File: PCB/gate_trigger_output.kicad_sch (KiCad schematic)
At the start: 9 parts, among them J2 OUTa, J3 OUTb, Q2 BC547

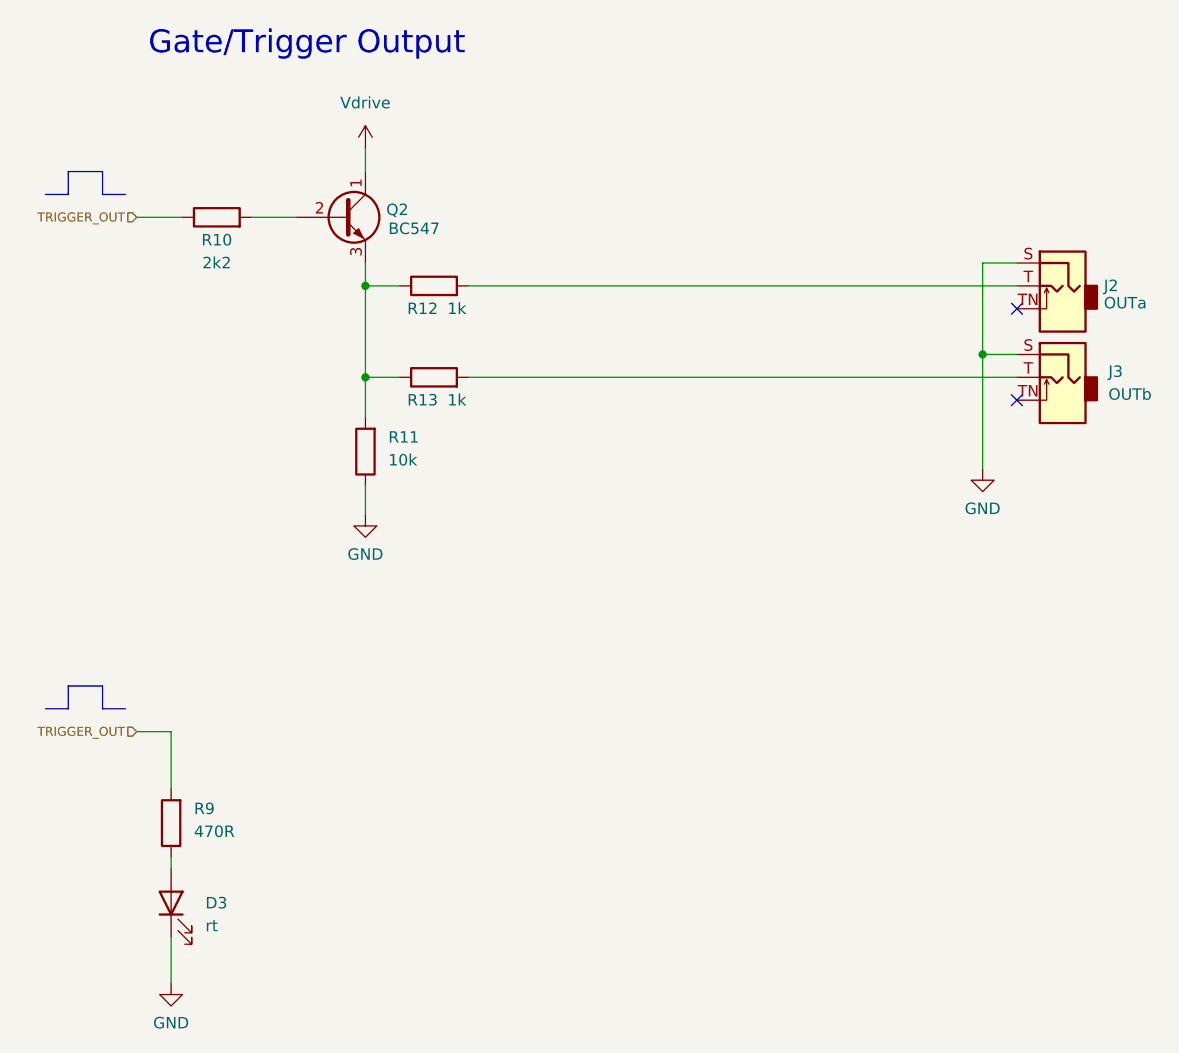
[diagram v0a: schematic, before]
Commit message: :memo: Geographically reannotate the PCB
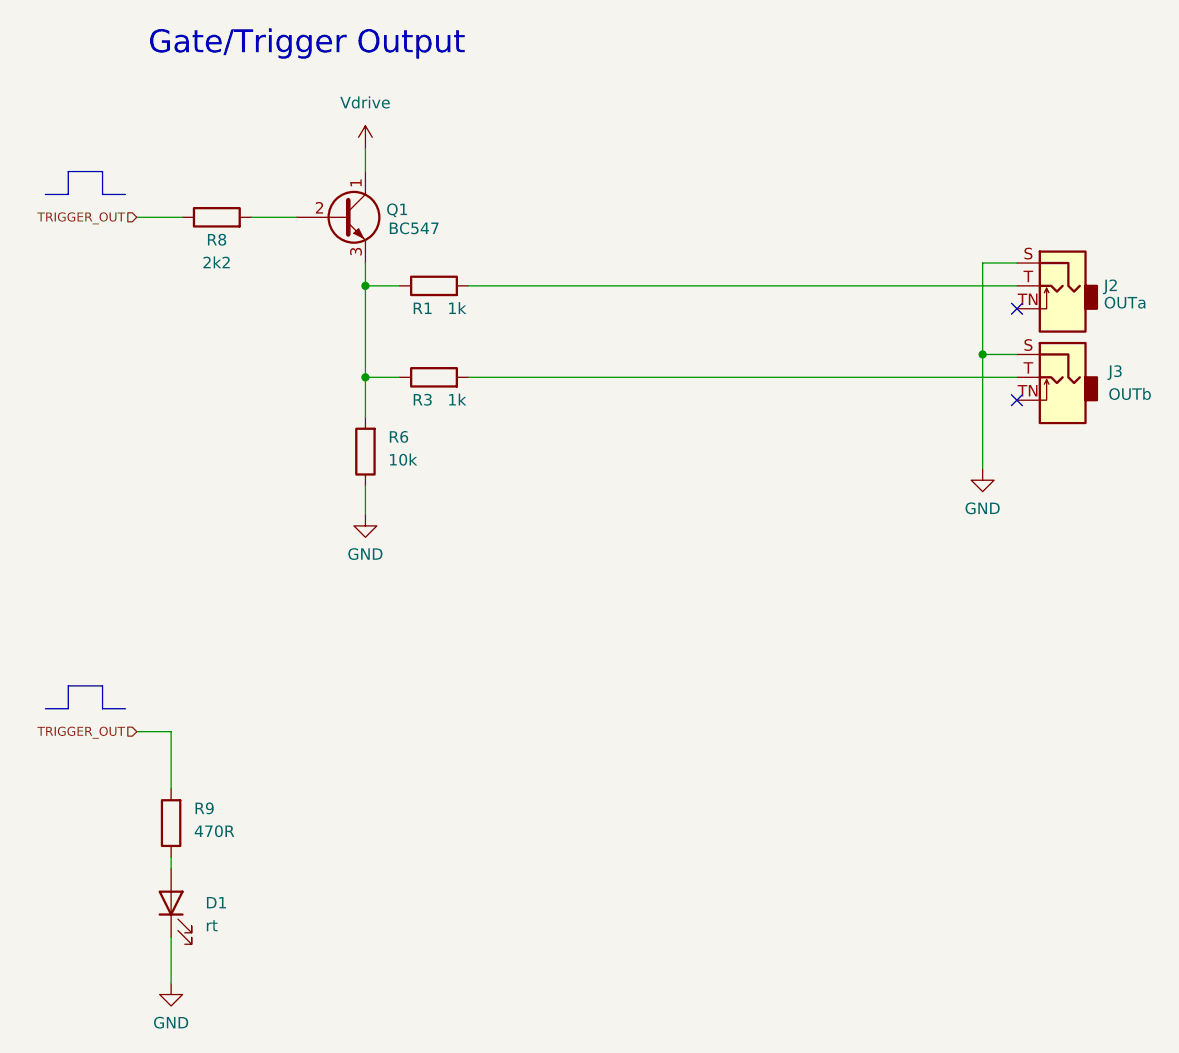
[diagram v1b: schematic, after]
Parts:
- renumbered D3 to D1, Q2 to Q1, R12 to R1, R13 to R3, R11 to R6, R10 to R8
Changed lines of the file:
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@@
         )
         (path "/64d6412c-bfad-42df-9ed7-bcc6cbff0470/b0ca186f-8794-49d8-ae6e-2d447887c3e3"
-          (reference "J8") (unit 1)
+          (reference "J9") (unit 1)
         )
       )
@@
   (symbol (lib_id "Device:R") (at 58.42 70.485 180) (unit 1)
     (in_bom yes) (on_board yes) (dnp no)
-    (property "Reference" "R11" (at 60.96 68.8975 0)
+    (property "Reference" "R6" (at 60.96 68.8975 0)
       (effects (font (size 1.27 1.27)) (justify right))
     )
@@
       (project "manual-gate-trigger-source"
         (path "/64d6412c-bfad-42df-9ed7-bcc6cbff0470/5e147908-dd0e-44a6-bf7b-e0f4f3b88ce0"
-          (reference "R11") (unit 1)
-        )
-        (path "/64d6412c-bfad-42df-9ed7-bcc6cbff0470/4d130511-3de2-468d-9ad3-9fd4dd47645e"
-          (reference "R16") (unit 1)
-        )
-        (path "/64d6412c-bfad-42df-9ed7-bcc6cbff0470/b83b5c1b-da69-40b5-857e-949eb4f1eab8"
-          (reference "R21") (unit 1)
-        )
-        (path "/64d6412c-bfad-42df-9ed7-bcc6cbff0470/b0ca186f-8794-49d8-ae6e-2d447887c3e3"
-          (reference "R26") (unit 1)
+          (reference "R6") (unit 1)
+        )
+        (path "/64d6412c-bfad-42df-9ed7-bcc6cbff0470/4d130511-3de2-468d-9ad3-9fd4dd47645e"
+          (reference "R19") (unit 1)
+        )
+        (path "/64d6412c-bfad-42df-9ed7-bcc6cbff0470/b83b5c1b-da69-40b5-857e-949eb4f1eab8"
+          (reference "R32") (unit 1)
+        )
+        (path "/64d6412c-bfad-42df-9ed7-bcc6cbff0470/b0ca186f-8794-49d8-ae6e-2d447887c3e3"
+          (reference "R38") (unit 1)
         )
       )
@@
   (symbol (lib_id "Transistor_BJT:BC547") (at 55.88 44.45 0) (unit 1)
     (in_bom yes) (on_board yes) (dnp no)
-    (property "Reference" "Q2" (at 60.7314 43.6153 0)
+    (property "Reference" "Q1" (at 60.7314 43.6153 0)
       (effects (font (size 1.27 1.27)) (justify left))
     )
@@
       (project "manual-gate-trigger-source"
         (path "/64d6412c-bfad-42df-9ed7-bcc6cbff0470/5e147908-dd0e-44a6-bf7b-e0f4f3b88ce0"
+          (reference "Q1") (unit 1)
+        )
+        (path "/64d6412c-bfad-42df-9ed7-bcc6cbff0470/4d130511-3de2-468d-9ad3-9fd4dd47645e"
           (reference "Q2") (unit 1)
         )
-        (path "/64d6412c-bfad-42df-9ed7-bcc6cbff0470/4d130511-3de2-468d-9ad3-9fd4dd47645e"
+        (path "/64d6412c-bfad-42df-9ed7-bcc6cbff0470/b83b5c1b-da69-40b5-857e-949eb4f1eab8"
           (reference "Q3") (unit 1)
         )
-        (path "/64d6412c-bfad-42df-9ed7-bcc6cbff0470/b83b5c1b-da69-40b5-857e-949eb4f1eab8"
+        (path "/64d6412c-bfad-42df-9ed7-bcc6cbff0470/b0ca186f-8794-49d8-ae6e-2d447887c3e3"
           (reference "Q4") (unit 1)
         )
-        (path "/64d6412c-bfad-42df-9ed7-bcc6cbff0470/b0ca186f-8794-49d8-ae6e-2d447887c3e3"
-          (reference "Q5") (unit 1)
-        )
       )
     )
@@
   (symbol (lib_id "Device:R") (at 41.91 44.45 90) (unit 1)
     (in_bom yes) (on_board yes) (dnp no)
-    (property "Reference" "R10" (at 41.91 46.99 90)
+    (property "Reference" "R8" (at 41.91 46.99 90)
       (effects (font (size 1.27 1.27)))
     )
@@
       (project "manual-gate-trigger-source"
         (path "/64d6412c-bfad-42df-9ed7-bcc6cbff0470/5e147908-dd0e-44a6-bf7b-e0f4f3b88ce0"
-          (reference "R10") (unit 1)
-        )
-        (path "/64d6412c-bfad-42df-9ed7-bcc6cbff0470/4d130511-3de2-468d-9ad3-9fd4dd47645e"
-          (reference "R15") (unit 1)
-        )
-        (path "/64d6412c-bfad-42df-9ed7-bcc6cbff0470/b83b5c1b-da69-40b5-857e-949eb4f1eab8"
-          (reference "R20") (unit 1)
-        )
-        (path "/64d6412c-bfad-42df-9ed7-bcc6cbff0470/b0ca186f-8794-49d8-ae6e-2d447887c3e3"
-          (reference "R25") (unit 1)
+          (reference "R8") (unit 1)
+        )
+        (path "/64d6412c-bfad-42df-9ed7-bcc6cbff0470/4d130511-3de2-468d-9ad3-9fd4dd47645e"
+          (reference "R13") (unit 1)
+        )
+        (path "/64d6412c-bfad-42df-9ed7-bcc6cbff0470/b83b5c1b-da69-40b5-857e-949eb4f1eab8"
+          (reference "R23") (unit 1)
+        )
+        (path "/64d6412c-bfad-42df-9ed7-bcc6cbff0470/b0ca186f-8794-49d8-ae6e-2d447887c3e3"
+          (reference "R30") (unit 1)
         )
       )
@@
   (symbol (lib_id "Device:R") (at 66.04 62.23 90) (unit 1)
     (in_bom yes) (on_board yes) (dnp no)
-    (property "Reference" "R13" (at 64.77 64.77 90)
+    (property "Reference" "R3" (at 64.77 64.77 90)
       (effects (font (size 1.27 1.27)))
     )
@@
       (project "manual-gate-trigger-source"
         (path "/64d6412c-bfad-42df-9ed7-bcc6cbff0470/5e147908-dd0e-44a6-bf7b-e0f4f3b88ce0"
-          (reference "R13") (unit 1)
-        )
-        (path "/64d6412c-bfad-42df-9ed7-bcc6cbff0470/4d130511-3de2-468d-9ad3-9fd4dd47645e"
-          (reference "R18") (unit 1)
-        )
-        (path "/64d6412c-bfad-42df-9ed7-bcc6cbff0470/b83b5c1b-da69-40b5-857e-949eb4f1eab8"
-          (reference "R23") (unit 1)
-        )
-        (path "/64d6412c-bfad-42df-9ed7-bcc6cbff0470/b0ca186f-8794-49d8-ae6e-2d447887c3e3"
-          (reference "R28") (unit 1)
+          (reference "R3") (unit 1)
+        )
+        (path "/64d6412c-bfad-42df-9ed7-bcc6cbff0470/4d130511-3de2-468d-9ad3-9fd4dd47645e"
+          (reference "R16") (unit 1)
+        )
+        (path "/64d6412c-bfad-42df-9ed7-bcc6cbff0470/b83b5c1b-da69-40b5-857e-949eb4f1eab8"
+          (reference "R26") (unit 1)
+        )
+        (path "/64d6412c-bfad-42df-9ed7-bcc6cbff0470/b0ca186f-8794-49d8-ae6e-2d447887c3e3"
+          (reference "R34") (unit 1)
         )
       )
@@
         )
         (path "/64d6412c-bfad-42df-9ed7-bcc6cbff0470/b83b5c1b-da69-40b5-857e-949eb4f1eab8"
-          (reference "R19") (unit 1)
-        )
-        (path "/64d6412c-bfad-42df-9ed7-bcc6cbff0470/b0ca186f-8794-49d8-ae6e-2d447887c3e3"
-          (reference "R24") (unit 1)
+          (reference "R22") (unit 1)
+        )
+        (path "/64d6412c-bfad-42df-9ed7-bcc6cbff0470/b0ca186f-8794-49d8-ae6e-2d447887c3e3"
+          (reference "R29") (unit 1)
         )
       )
@@
         )
         (path "/64d6412c-bfad-42df-9ed7-bcc6cbff0470/b0ca186f-8794-49d8-ae6e-2d447887c3e3"
-          (reference "J9") (unit 1)
+          (reference "J10") (unit 1)
         )
       )
@@
   (symbol (lib_id "Device:LED") (at 36.83 120.65 90) (unit 1)
     (in_bom yes) (on_board yes) (dnp no)
-    (property "Reference" "D3" (at 40.64 120.65 90)
+    (property "Reference" "D1" (at 40.64 120.65 90)
       (effects (font (size 1.27 1.27)) (justify right))
     )
@@
       (project "manual-gate-trigger-source"
         (path "/64d6412c-bfad-42df-9ed7-bcc6cbff0470/5e147908-dd0e-44a6-bf7b-e0f4f3b88ce0"
+          (reference "D1") (unit 1)
+        )
+        (path "/64d6412c-bfad-42df-9ed7-bcc6cbff0470/4d130511-3de2-468d-9ad3-9fd4dd47645e"
+          (reference "D2") (unit 1)
+        )
+        (path "/64d6412c-bfad-42df-9ed7-bcc6cbff0470/b83b5c1b-da69-40b5-857e-949eb4f1eab8"
           (reference "D3") (unit 1)
         )
-        (path "/64d6412c-bfad-42df-9ed7-bcc6cbff0470/4d130511-3de2-468d-9ad3-9fd4dd47645e"
-          (reference "D4") (unit 1)
-        )
-        (path "/64d6412c-bfad-42df-9ed7-bcc6cbff0470/b83b5c1b-da69-40b5-857e-949eb4f1eab8"
-          (reference "D5") (unit 1)
-        )
         (path "/64d6412c-bfad-42df-9ed7-bcc6cbff0470/b0ca186f-8794-49d8-ae6e-2d447887c3e3"
           (reference "D6") (unit 1)
@@
   (symbol (lib_id "Device:R") (at 66.04 52.07 90) (unit 1)
     (in_bom yes) (on_board yes) (dnp no)
-    (property "Reference" "R12" (at 64.77 54.61 90)
+    (property "Reference" "R1" (at 64.77 54.61 90)
       (effects (font (size 1.27 1.27)))
     )
@@
       (project "manual-gate-trigger-source"
         (path "/64d6412c-bfad-42df-9ed7-bcc6cbff0470/5e147908-dd0e-44a6-bf7b-e0f4f3b88ce0"
-          (reference "R12") (unit 1)
-        )
-        (path "/64d6412c-bfad-42df-9ed7-bcc6cbff0470/4d130511-3de2-468d-9ad3-9fd4dd47645e"
-          (reference "R17") (unit 1)
-        )
-        (path "/64d6412c-bfad-42df-9ed7-bcc6cbff0470/b83b5c1b-da69-40b5-857e-949eb4f1eab8"
-          (reference "R22") (unit 1)
-        )
-        (path "/64d6412c-bfad-42df-9ed7-bcc6cbff0470/b0ca186f-8794-49d8-ae6e-2d447887c3e3"
-          (reference "R27") (unit 1)
-        )
-      )
+          (reference "R1") (unit 1)
+        )
+        (path "/64d6412c-bfad-42df-9ed7-bcc6cbff0470/4d130511-3de2-468d-9ad3-9fd4dd47645e"
+          (reference "R11") (unit 1)
+        )
+        (path "/64d6412c-bfad-42df-9ed7-bcc6cbff0470/b83b5c1b-da69-40b5-857e-949eb4f1eab8"
+          (reference "R21") (unit 1)
+        )
+        (path "/64d6412c-bfad-42df-9ed7-bcc6cbff0470/b0ca186f-8794-49d8-ae6e-2d447887c3e3"
+          (reference "R33") (unit 1)
+        )
+      )
